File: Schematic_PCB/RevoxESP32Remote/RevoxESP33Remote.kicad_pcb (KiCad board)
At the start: 2 copper layers, 124.5 x 73.7 mm, 34 parts, among them J1 SerialLink, J2 Conn_01x04, J3 Conn_01x10, J4 Conn_01x05, J5 Conn_01x04, J6 Conn_01x03, J7 Conn_01x03, Q1 BC550, Q2 2N2222, Q3 BC550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

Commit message: N.V.
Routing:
- net +5V: track 0.00 -> 305.7 mm
- net Net-(D1-K): track 0.00 -> 179.5 mm
- net +3V3: track 0.00 -> 134.0 mm, vias 0 -> 1
- net IRrecv: track 0.00 -> 104.8 mm, vias 0 -> 1
- net IO32: track 0.00 -> 100.0 mm
- net IO02: track 0.00 -> 98.6 mm, vias 0 -> 1
- net IO04: track 0.00 -> 86.6 mm, vias 0 -> 1
- net RevoxTTL_RXD: track 0.00 -> 82.7 mm
- net IO33: track 0.00 -> 75.1 mm, vias 0 -> 3
- net RevoxTTL_TXD: track 0.00 -> 73.5 mm
- net IO23: track 0.00 -> 65.7 mm, vias 0 -> 1
- net TTL_RTS: track 0.00 -> 62.8 mm, vias 0 -> 1
- net TTL_CTS: track 0.00 -> 62.0 mm, vias 0 -> 1
- net IO34: track 0.00 -> 61.7 mm, vias 0 -> 1
- net IO13: track 0.00 -> 60.7 mm, vias 0 -> 1
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
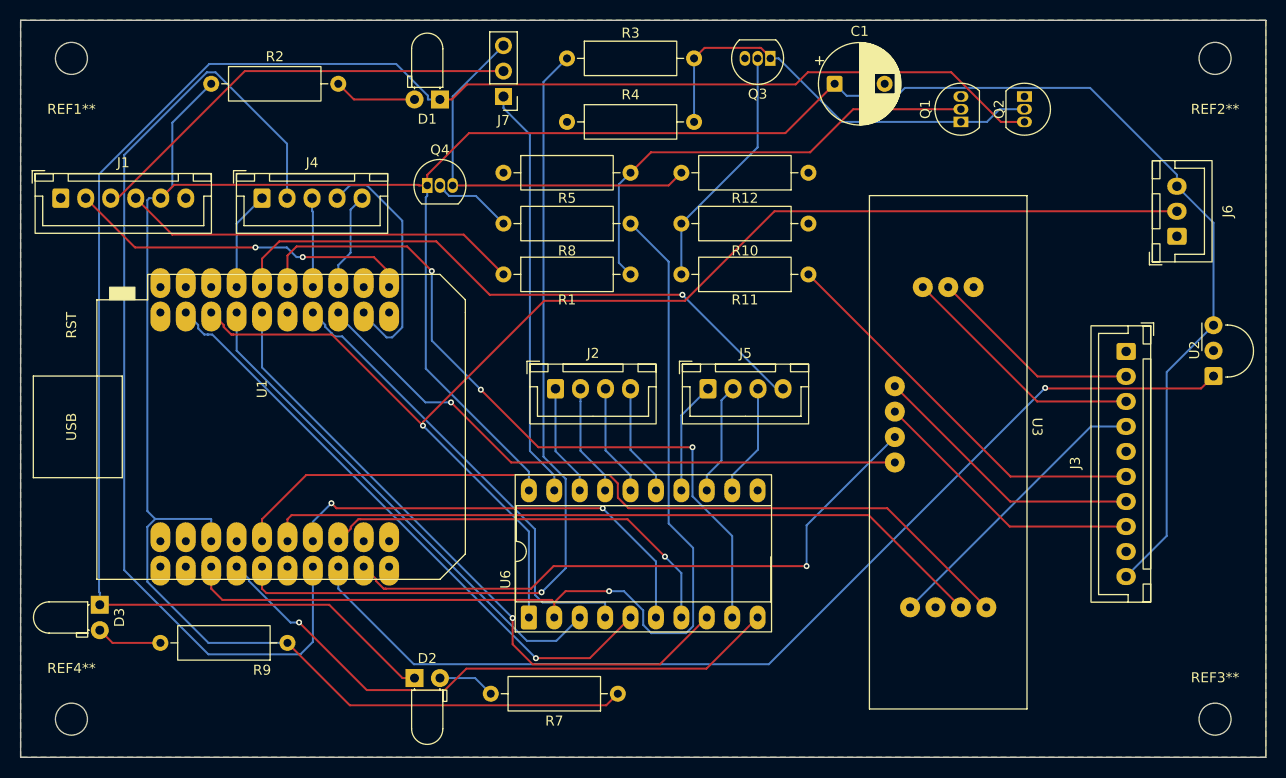
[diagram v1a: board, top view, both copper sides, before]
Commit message: sendIR durch sendRevoxFrame ersetzt. Leiterplatte eneuert.
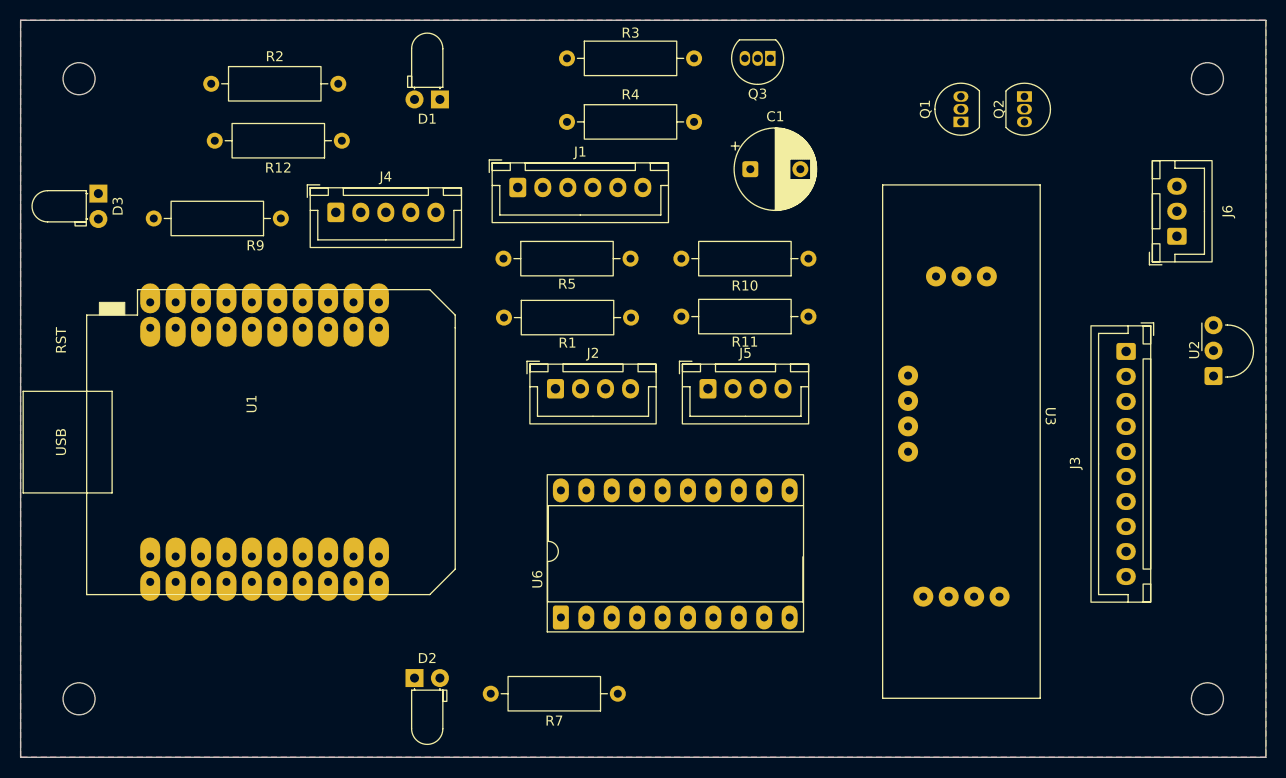
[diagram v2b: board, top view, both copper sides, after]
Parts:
- removed J7: Conn_01x03, Connector_PinHeader_2.54mm:PinHeader_1x03_P2.54mm_Vertical
- removed Q4: BC550, Package_TO_SOT_THT:TO-92_Inline
- removed R8: 10k, Resistor_THT:R_Axial_DIN0309_L9.0mm_D3.2mm_P12.70mm_Horizontal
- R12: value 10k -> 2,2k
- moved R12 46.7 mm to (114.7, 74.3)
- moved J1 45.7 mm to (132.2, 78.9)
- moved R9 42.4 mm to (108.6, 82.0)
- moved D3 41.1 mm to (90.3, 79.6)
- moved C1 12.0 mm to (155.5, 77.1)
- moved R5 8.59 mm to (130.8, 86.1)
- moved J4 7.51 mm to (114.1, 81.4)
- moved R1 4.32 mm to (130.9, 91.9)
- moved R11 4.22 mm to (161.3, 91.8)
- moved R10 3.51 mm to (161.3, 86.1)
- moved U6 3.20 mm to (136.6, 121.9)
- moved REF3** 2.17 mm to (201.2, 130.0)
- moved REF4** 2.17 mm to (88.4, 130.0)
- moved REF1** 2.17 mm to (88.4, 68.1)
- moved REF2** 2.17 mm to (201.2, 68.1)
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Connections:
- R12 pad 1: GND -> SerialLink
- R12 pad 2: IO05_OUT -> GND
- U6 pad 19: B0_TTL5V -> SerialLink
- U6 pad 2: IO02 -> IO05
- U6 pad 3: IO05 -> IO02
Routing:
- net +5V: track 305.7 -> 0.00 mm
- net Net-(D1-K): track 179.5 -> 0.00 mm
- net +3V3: track 134.0 -> 0.00 mm, vias 1 -> 0
- net IRrecv: track 104.8 -> 0.00 mm, vias 1 -> 0
- net IO32: track 100.0 -> 0.00 mm
- net IO02: track 98.6 -> 0.00 mm, vias 1 -> 0
- net IO04: track 86.6 -> 0.00 mm, vias 1 -> 0
- net RevoxTTL_RXD: track 82.7 -> 0.00 mm
- net IO33: track 75.1 -> 0.00 mm, vias 3 -> 0
- net RevoxTTL_TXD: track 73.5 -> 0.00 mm
- net IO23: track 65.7 -> 0.00 mm, vias 1 -> 0
- net TTL_RTS: track 62.8 -> 0.00 mm, vias 1 -> 0
- net TTL_CTS: track 62.0 -> 0.00 mm, vias 1 -> 0
- net IO34: track 61.7 -> 0.00 mm, vias 1 -> 0
- net IO13: track 60.7 -> 0.00 mm, vias 1 -> 0
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
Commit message: Leiterplattendaten erneuert.
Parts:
- moved U2 3.33 mm to (202.2, 101.1)
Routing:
- net +5V: track 0.00 -> 262.6 mm
- net Net-(D1-K): track 0.00 -> 158.3 mm
- net +3V3: track 0.00 -> 144.0 mm, vias 0 -> 1
- net IRrecv: track 0.00 -> 131.1 mm
- net IO04: track 0.00 -> 95.7 mm
- net IO33: track 0.00 -> 80.3 mm, vias 0 -> 1
- net RevoxTTL_RXD: track 0.00 -> 80.2 mm
- net RevoxTTL_TXD: track 0.00 -> 74.8 mm
- net TTL_RTS: track 0.00 -> 73.5 mm, vias 0 -> 1
- net IO32: track 0.00 -> 68.7 mm, vias 0 -> 2
- net IO13: track 0.00 -> 64.6 mm, vias 0 -> 1
- net TTL_CTS: track 0.00 -> 64.4 mm
- net IO23: track 0.00 -> 63.1 mm, vias 0 -> 1
- net IO34: track 0.00 -> 62.2 mm
- net IO00: track 0.00 -> 61.5 mm, vias 0 -> 2
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
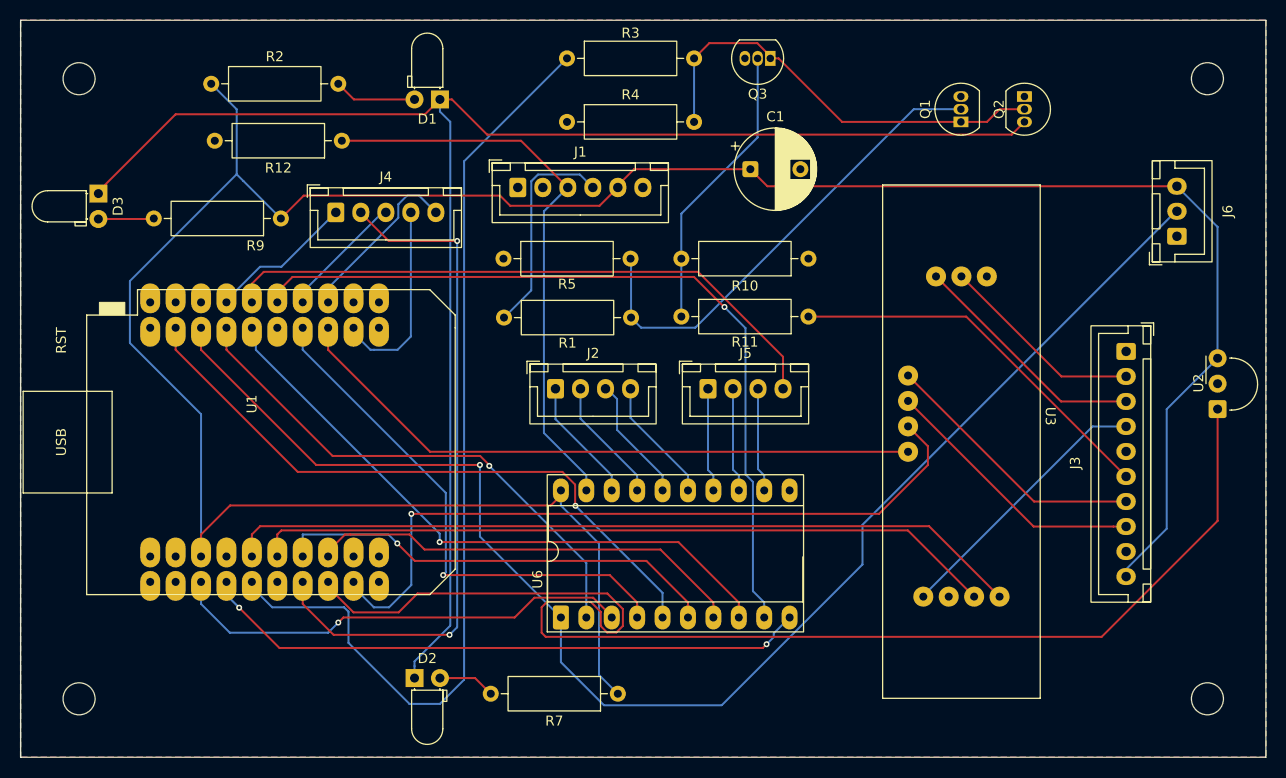
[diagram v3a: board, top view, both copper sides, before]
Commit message: Bugfix: Einige verbesserungen im Javascript, 0X wurde nicht korrekt ausgeführt.
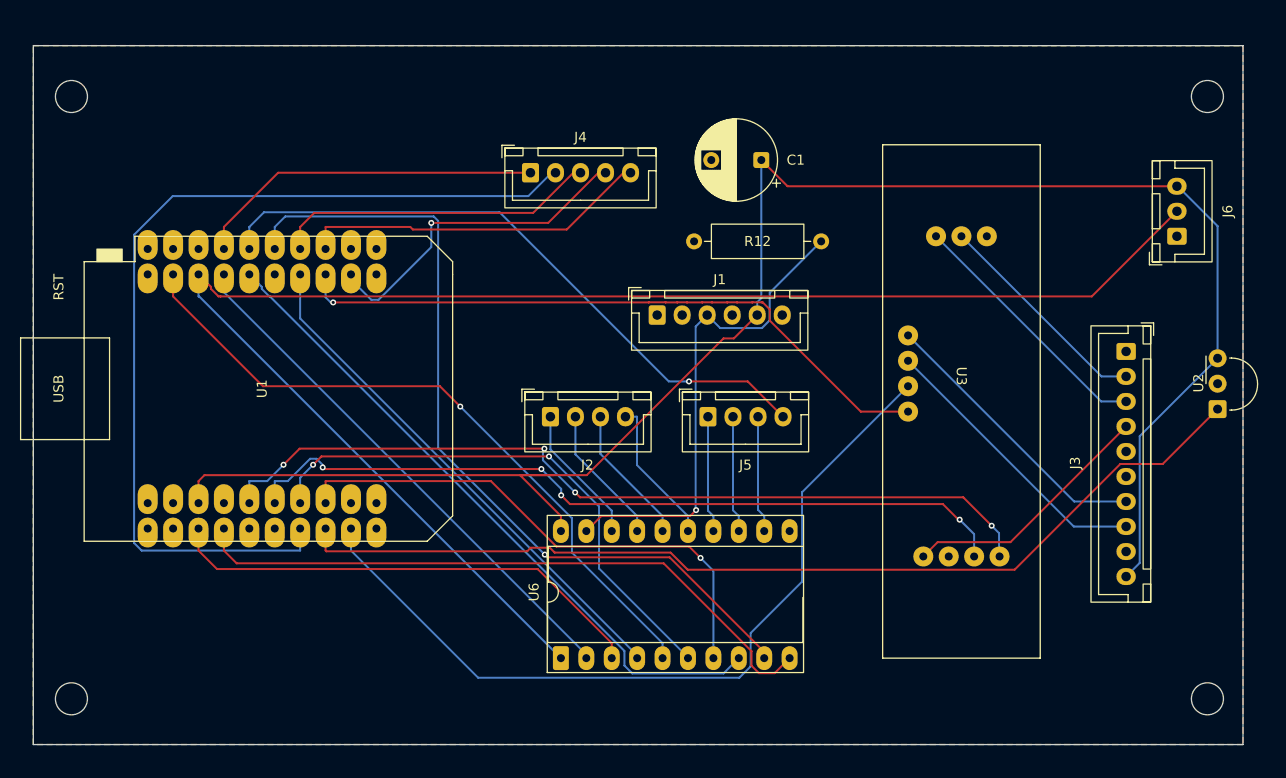
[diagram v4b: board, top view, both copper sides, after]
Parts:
- removed D1, D2, D3: LED, LED_THT:LED_D3.0mm_Horizontal_O1.27mm_Z2.0mm_IRBlack
- removed Q1, Q3: BC550, Package_TO_SOT_THT:TO-92_Inline
- removed Q2: 2N2222, Package_TO_SOT_THT:TO-92_Inline
- removed R1, R11, R3: 4,7k, Resistor_THT:R_Axial_DIN0309_L9.0mm_D3.2mm_P12.70mm_Horizontal
- removed R10, R4, R5: 22k, Resistor_THT:R_Axial_DIN0309_L9.0mm_D3.2mm_P12.70mm_Horizontal
- removed R2, R7, R9: 180, Resistor_THT:R_Axial_DIN0309_L9.0mm_D3.2mm_P12.70mm_Horizontal
- R12: value 2,2k -> 1k
- moved R12 48.9 mm to (162.6, 84.3)
- moved J4 19.9 mm to (133.5, 77.5)
- moved J1 18.9 mm to (146.2, 91.7)
- moved U1 5.34 mm to (106.7, 99.1)
- moved U6 4.06 mm to (136.6, 126.0)
- moved U3 4.01 mm to (176.6, 97.8)
- moved J2 2.84 mm to (135.5, 101.9)
- moved J5 2.79 mm to (151.2, 101.9)
- moved REF1** 1.93 mm to (87.6, 69.8)
- moved REF2** 1.78 mm to (201.2, 69.8)
- moved C1 1.43 mm to (156.6, 76.2), turned to 180 degrees
- moved REF4** 0.76 mm to (87.6, 130.0)
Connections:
- J1 pad 4: ~{EN1} -> unconnected-(J1-Pin_4-Pad4)
- J3 pad 6: ~{EN2} -> unconnected-(J3-Pin_6-Pad6)
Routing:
- net Net-(D1-K): track 158.3 -> 0.00 mm
- net IO04: track 95.7 -> 0.00 mm
- net +5V: track 262.6 -> 178.3 mm
- net Net-(Q1-B): track 48.3 -> 0.00 mm
- net Net-(Q1-C): track 43.9 -> 0.00 mm
- net ~{EN2}: track 38.4 -> 0.00 mm
- net IRrecv: track 131.1 -> 99.1 mm
- net Net-(Q3-B): track 29.0 -> 0.00 mm
- net IO32: track 68.7 -> 94.6 mm, vias 2 -> 0
- net ~{EN1}: track 21.7 -> 0.00 mm
- net IO14: track 14.8 -> 35.1 mm
- net IO35: track 12.6 -> 32.5 mm
- net IO39: track 17.5 -> 35.1 mm
- net IO36: track 19.9 -> 33.5 mm, vias 0 -> 1
- net +3V3: track 144.0 -> 155.7 mm, vias 1 -> 0
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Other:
- board size 124.5 x 73.7 mm -> 120.9 x 69.9 mm
